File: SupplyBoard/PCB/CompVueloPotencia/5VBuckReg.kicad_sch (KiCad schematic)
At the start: 11 parts, among them U11 TPS5430DDA

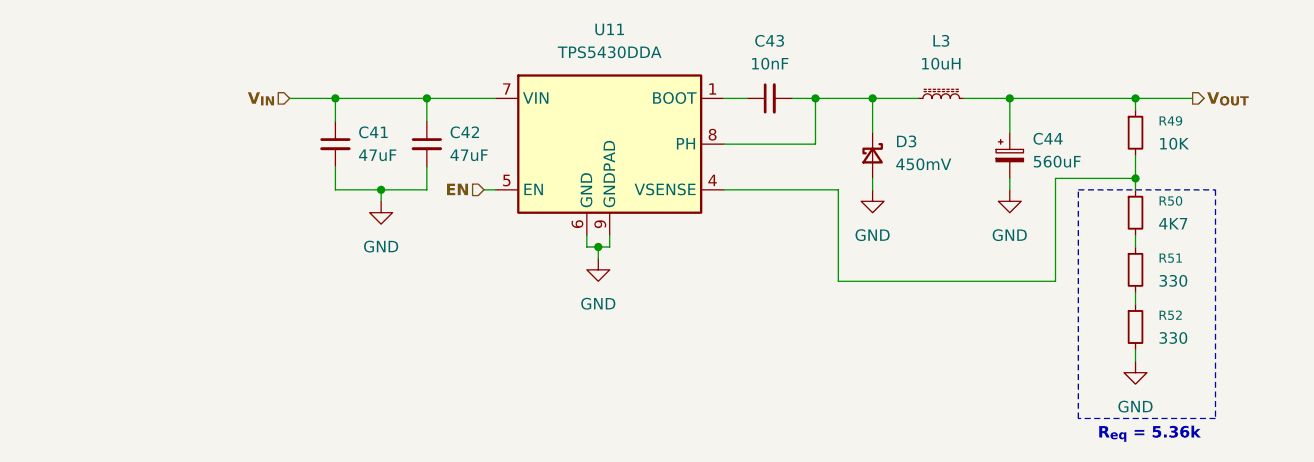
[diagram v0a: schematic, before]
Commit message: SupplyBoard - update layout
schematic completed and PCB layout started; only the routing of the traces remains to be done
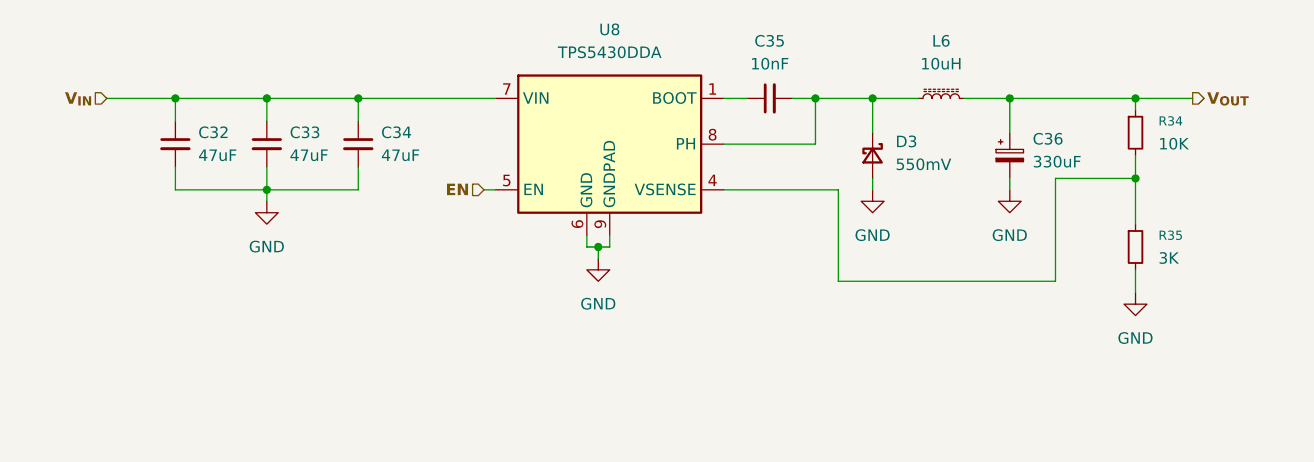
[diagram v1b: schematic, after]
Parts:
- removed R51, R52: 330, symbol Device:R_Small
- added C32: 47uF, Capacitor_SMD:C_0805_2012Metric_Pad1.18x1.45mm_HandSolder, symbol Device:C_Small
- C33: renamed from C41; footprint (none) -> Capacitor_SMD:C_0805_2012Metric_Pad1.18x1.45mm_HandSolder
- C34: renamed from C42; footprint (none) -> Capacitor_SMD:C_0805_2012Metric_Pad1.18x1.45mm_HandSolder
- C35: renamed from C43; footprint (none) -> Capacitor_SMD:C_0805_2012Metric_Pad1.18x1.45mm_HandSolder
- C36: renamed from C44; value 560uF -> 330uF; footprint (none) -> Capacitor_Tantalum_SMD:CP_EIA-7343-31_Kemet-D_HandSolder
- D3: value 450mV -> 550mV; footprint (none) -> Diode_SMD:D_SMA-SMB_Universal_Handsoldering
- L6: renamed from L3; footprint (none) -> Inductor_SMD:L_Bourns_SRN6045TA
- R34: renamed from R49; footprint (none) -> Resistor_SMD:R_0805_2012Metric_Pad1.20x1.40mm_HandSolder
- R35: renamed from R50; value 4K7 -> 3K; footprint (none) -> Resistor_SMD:R_0805_2012Metric_Pad1.20x1.40mm_HandSolder
- U8: renamed from U11; footprint Package_SO:TI_SO-PowerPAD-8_ThermalVias -> CompVuelo:Texas_S-PDSO-G8_3x3mm_P0.65mm
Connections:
- net GND: now also R35.2, C32.2
- net V_{IN}: now also C32.1
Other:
- note removed: "R_{eq} = 5.36k"
- moved on the sheet: C33, C34, R35
